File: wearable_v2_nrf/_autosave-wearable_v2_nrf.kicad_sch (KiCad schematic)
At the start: 54 parts, among them IC1 MCP73831T-2ACI_OT, J1 Conn_01x04, J2 217175-0001, J3 Conn_01x03, M1 Motor_DC, Q1 PMOS, Q2 NPN, SW1 Reset, U1 nRF52811-QCxx, U3 BMI270, U4 MCP1700x-330xxMB, U5 2450AT18A100E, Y1 ABM10W-32.0000MHZ-8-B1U-T3, Y2 Crystal

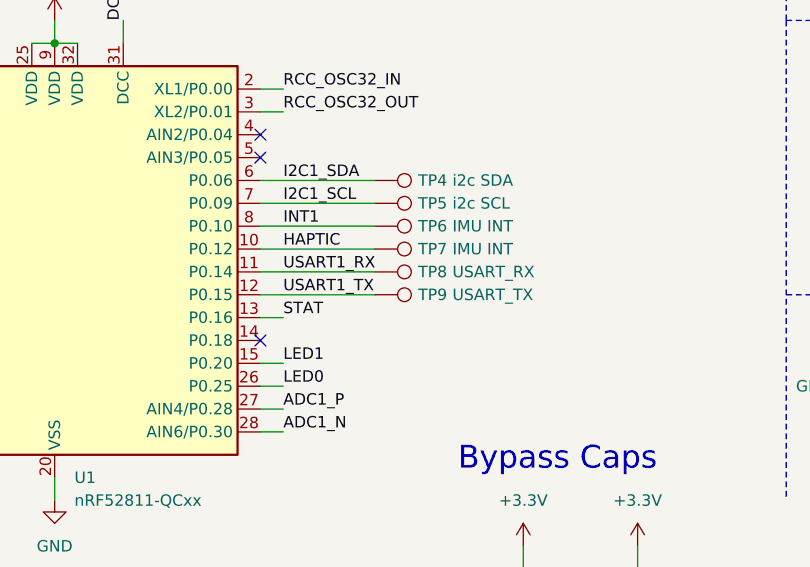
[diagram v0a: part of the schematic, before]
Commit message: finished nrf schematic/layout 👷‍♂️
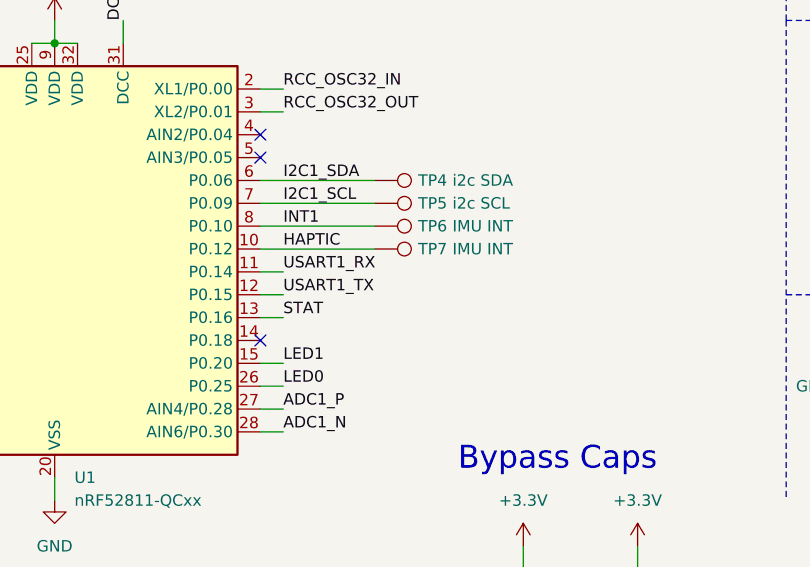
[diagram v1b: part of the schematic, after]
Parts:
- removed TP8: USART_RX, TestPoint:TestPoint_THTPad_1.5x1.5mm_Drill0.7mm, symbol Connector:TestPoint
- removed TP9: USART_TX, TestPoint:TestPoint_THTPad_1.5x1.5mm_Drill0.7mm, symbol Connector:TestPoint
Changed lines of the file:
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@@
 	(wire
 		(pts
-			(xy 214.63 142.24) (xy 214.63 144.78)
+			(xy 172.72 114.3) (xy 175.26 114.3)
 		)
 		(stroke
@@
 	(wire
 		(pts
-			(xy 201.93 152.4) (xy 201.93 154.94)
+			(xy 214.63 142.24) (xy 214.63 144.78)
 		)
 		(stroke
@@
 	(wire
 		(pts
-			(xy 176.53 27.94) (xy 177.8 27.94)
+			(xy 201.93 152.4) (xy 201.93 154.94)
 		)
 		(stroke
@@
 	(wire
 		(pts
-			(xy 172.72 121.92) (xy 175.26 121.92)
+			(xy 176.53 27.94) (xy 177.8 27.94)
 		)
 		(stroke
@@
 	(wire
 		(pts
-			(xy 166.37 36.83) (xy 177.8 36.83)
+			(xy 172.72 121.92) (xy 175.26 121.92)
 		)
 		(stroke
@@
 	(wire
 		(pts
-			(xy 124.46 124.46) (xy 127 124.46)
+			(xy 166.37 36.83) (xy 177.8 36.83)
 		)
 		(stroke
@@
 	(wire
 		(pts
-			(xy 245.11 137.16) (xy 245.11 135.89)
+			(xy 124.46 124.46) (xy 127 124.46)
 		)
 		(stroke
@@
 	(wire
 		(pts
-			(xy 172.72 114.3) (xy 185.42 114.3)
+			(xy 245.11 137.16) (xy 245.11 135.89)
 		)
 		(stroke
@@
 	(wire
 		(pts
-			(xy 172.72 111.76) (xy 185.42 111.76)
+			(xy 67.31 187.325) (xy 67.31 189.23)
 		)
 		(stroke
@@
 	(wire
 		(pts
-			(xy 67.31 187.325) (xy 67.31 189.23)
+			(xy 172.72 111.76) (xy 175.26 111.76)
 		)
 		(stroke
@@
 	)
 	(symbol
-		(lib_id "Connector:TestPoint")
-		(at 185.42 111.76 270)
-		(unit 1)
-		(exclude_from_sim no)
-		(in_bom yes)
-		(on_board yes)
-		(dnp no)
-		(property "Reference" "TP8"
-			(at 190.246 111.76 90)
-			(effects
-				(font
-					(size 1.27 1.27)
-				)
-				(justify left)
-			)
-		)
-		(property "Value" "USART_RX"
-			(at 194.056 111.76 90)
-			(effects
-				(font
-					(size 1.27 1.27)
-				)
-				(justify left)
-			)
-		)
-		(property "Footprint" "TestPoint:TestPoint_THTPad_1.5x1.5mm_Drill0.7mm"
-			(at 185.42 116.84 0)
-			(effects
-				(font
-					(size 1.27 1.27)
-				)
-				(hide yes)
-			)
-		)
-		(property "Datasheet" "~"
-			(at 185.42 116.84 0)
-			(effects
-				(font
-					(size 1.27 1.27)
-				)
-				(hide yes)
-			)
-		)
-		(property "Description" "test point"
-			(at 185.42 111.76 0)
-			(effects
-				(font
-					(size 1.27 1.27)
-				)
-				(hide yes)
-			)
-		)
-		(pin "1"
-		)
-		(instances
-			(project "wearable_v2_nrf"
-				(path "/04076b6c-00f0-4736-97bb-31ddf474c7f4"
-					(reference "TP8")
-					(unit 1)
-				)
-			)
-		)
-	)
-	(symbol
 		(lib_id "Diode:1N4148")
 		(at 132.08 168.91 270)
@@
 					(unit 1)
 				)
-			)
-		)
-	)
-	(symbol
-		(lib_id "Connector:TestPoint")
-		(at 185.42 114.3 270)
-		(unit 1)
-		(exclude_from_sim no)
-		(in_bom yes)
-		(on_board yes)
-		(dnp no)
-		(property "Reference" "TP9"
-			(at 190.246 114.3 90)
-			(effects
-				(font
-					(size 1.27 1.27)
-				)
-				(justify left)
-			)
-		)
-		(property "Value" "USART_TX"
-			(at 194.056 114.3 90)
-			(effects
-				(font
-					(size 1.27 1.27)
-				)
-				(justify left)
-			)
-		)
-		(property "Footprint" "TestPoint:TestPoint_THTPad_1.5x1.5mm_Drill0.7mm"
-			(at 185.42 119.38 0)
-			(effects
-				(font
-					(size 1.27 1.27)
-				)
-				(hide yes)
-			)
-		)
-		(property "Datasheet" "~"
-			(at 185.42 119.38 0)
-			(effects
-				(font
-					(size 1.27 1.27)
-				)
-				(hide yes)
-			)
-		)
-		(property "Description" "test point"
-			(at 185.42 114.3 0)
-			(effects
-				(font
-					(size 1.27 1.27)
-				)
-				(hide yes)
-			)
-		)
-		(pin "1"
-		)
-		(instances
-			(project "wearable_v2_nrf"
-				(path "/04076b6c-00f0-4736-97bb-31ddf474c7f4"
-					(reference "TP9")
-					(unit 1)
-				)
